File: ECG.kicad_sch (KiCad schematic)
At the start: 0 parts

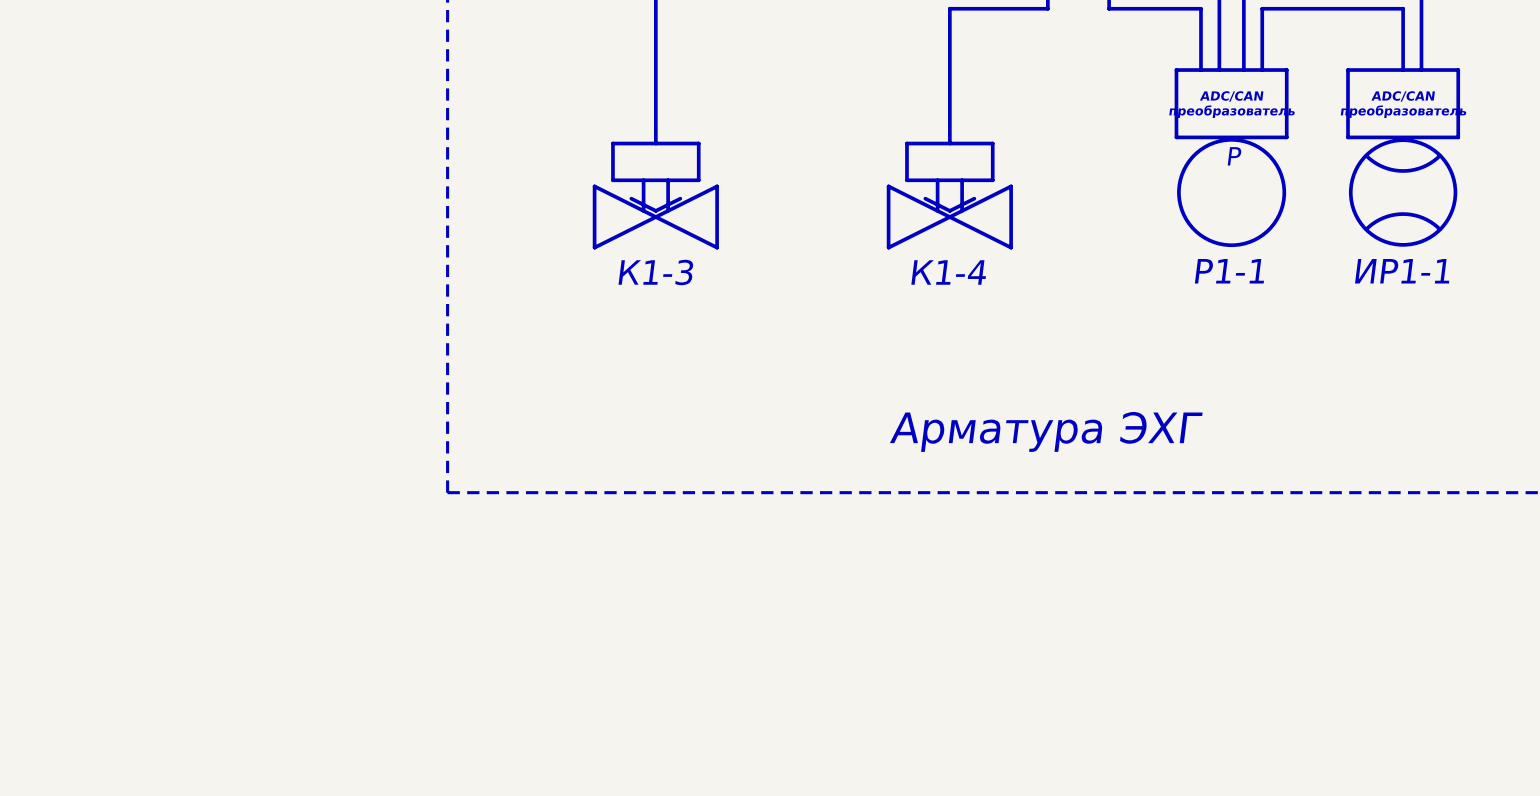
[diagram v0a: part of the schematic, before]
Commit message: VER1.0: добавил схему в пдф
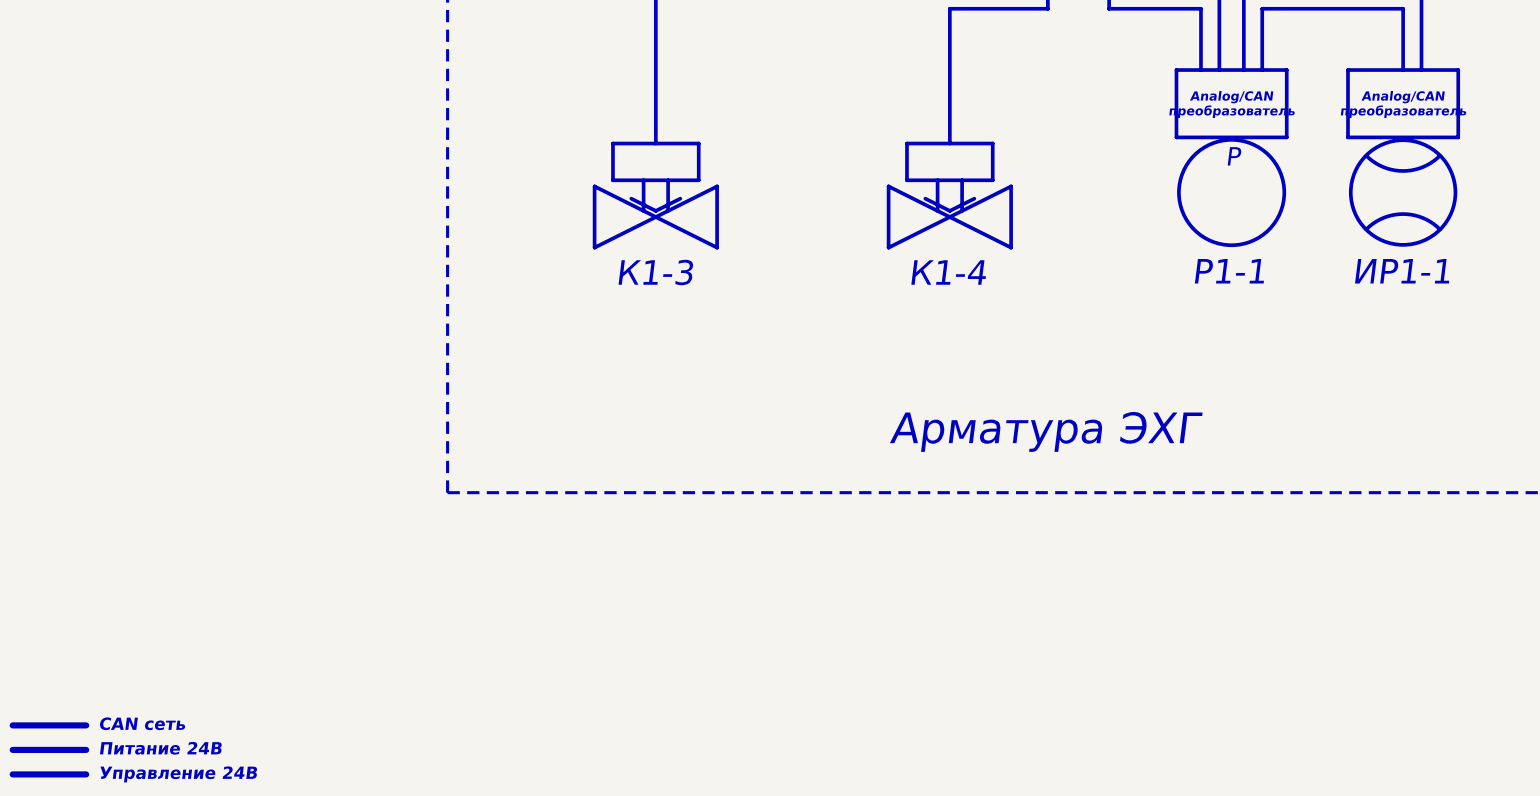
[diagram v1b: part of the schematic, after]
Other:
- note added: "Питание 24В"
- note added: "Управление 24В"
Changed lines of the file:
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@@
+		)
+	)
+	(text "Питание 24В"
+		(exclude_from_sim no)
+		(at 62.23 377.19 0)
+		(effects
+			(font
+				(face "Calibri")
+				(size 2.54 2.54)
+				(thickness 0.254)
+				(bold yes)
+				(italic yes)
+				(color 0 0 0 1)
+			)
+			(justify left)
 		)
 	)
@@
 		)
 	)
+	(text "Управление 24В"
+		(exclude_from_sim no)
+		(at 62.23 382.27 0)
+		(effects
+			(font
+				(face "Calibri")
+				(size 2.54 2.54)
+				(thickness 0.254)
+				(bold yes)
+				(italic yes)
+				(color 0 0 0 1)
+			)
+			(justify left)
+		)
+	)
+	(text "CAN сеть"
+		(exclude_from_sim no)
+		(at 62.23 372.11 0)
+		(effects
+			(font
+				(face "Calibri")
+				(size 2.54 2.54)
+				(thickness 0.254)
+				(bold yes)
+				(italic yes)
+				(color 0 0 0 1)
+			)
+			(justify left)
+		)
+	)
 	(text "ИР1-1"
 		(exclude_from_sim no)
@@
 		)
 	)
-	(text_box "ADC/CAN\nпреобразователь"
+	(text_box "Analog/CAN\nпреобразователь"
 		(exclude_from_sim no)
 		(at 321.31 236.22 0)
@@
 		)
 	)
-	(text_box "ADC/CAN\nпреобразователь"
+	(text_box "Analog/CAN\nпреобразователь"
 		(exclude_from_sim no)
 		(at 285.75 236.22 0)
@@
 	(polyline
 		(pts
+			(xy 44.45 382.27) (xy 59.69 382.27)
+		)
+		(stroke
+			(width 1.27)
+			(type solid)
+			(color 0 0 255 1)
+		)
+	)
+	(polyline
+		(pts
 			(xy 320.04 147.32) (xy 383.54 147.32)
 		)
@@
 	(polyline
 		(pts
+			(xy 44.45 372.11) (xy 59.69 372.11)
+		)
+		(stroke
+			(width 1.27)
+			(type solid)
+			(color 0 194 0 1)
+		)
+	)
+	(polyline
+		(pts
 			(xy 190.5 273.05) (xy 190.5 260.35)
 		)
@@
 		)
 	)
+	(polyline
+		(pts
+			(xy 44.45 377.19) (xy 59.69 377.19)
+		)
+		(stroke
+			(width 1.27)
+			(type solid)
+			(color 194 0 0 1)
+		)
+	)

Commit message: VER1.0: исправил часть замечаний по схеме
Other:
- note added: "220В"
- note added: "T"
- note added: "T2-1"
- note added: "Аналоговый сигнал"
- note added: "Напряжение переменное AC (сеть)"
- note added: "ЭН2-1"

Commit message: refactor for new ver
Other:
- note added: "Помещение 1"
- note added: "Помещение 2"
- note removed: "+24В"
- note removed: "Арматура ЭХГ"
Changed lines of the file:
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@@
+		)
+	)
+	(rectangle
+		(start 134.62 87.63)
+		(end 473.71 203.2)
+		(stroke
+			(width 0.635)
+			(type dash)
+			(color 0 0 0 1)
+		)
+		(fill
+			(type none)
 		)
 	)
@@
 		)
 	)
-	(text "+24В"
-		(exclude_from_sim no)
-		(at 350.52 160.528 0)
-		(effects
-			(font
-				(face "Calibri")
-				(size 3.81 3.81)
-				(italic yes)
-				(color 0 0 0 1)
-			)
-		)
-	)
 	(text "T2-1"
 		(exclude_from_sim no)
@@
 		)
 	)
+	(text "Помещение 1"
+		(exclude_from_sim no)
+		(at 435.864 100.33 0)
+		(effects
+			(font
+				(face "Calibri")
+				(size 6.35 6.35)
+				(italic yes)
+				(color 0 0 0 1)
+			)
+		)
+	)
 	(text "Напряжение переменное AC (сеть)"
 		(exclude_from_sim no)
@@
 		)
 	)
-	(text "CAN сеть"
-		(exclude_from_sim no)
-		(at 350.012 144.018 0)
-		(effects
-			(font
-				(face "Calibri")
-				(size 3.81 3.81)
-				(italic yes)
-				(color 0 0 0 1)
-			)
-		)
-	)
-	(text "Арматура ЭХГ"
-		(exclude_from_sim no)
-		(at 258.572 310.896 0)
+	(text "Помещение 2"
+		(exclude_from_sim no)
+		(at 440.436 316.23 0)
 		(effects
 			(font
@@
 	(text_box "Контроллер верхнего уровня (КВУ)"
 		(exclude_from_sim no)
-		(at 241.3 121.92 0)
+		(at 229.87 121.92 0)
 		(size 78.74 71.12)
 		(margins 0.9525 0.9525 0.9525 0.9525)
@@
 			(width 1.27)
 			(type solid)
-			(color 194 0 194 1)
+			(color 50 0 50 1)
 		)
 	)
@@
 	(polyline
 		(pts
-			(xy 320.04 163.83) (xy 383.54 163.83)
+			(xy 177.8 251.46) (xy 177.8 218.44)
+		)
+		(stroke
+			(width 0.762)
+			(type solid)
+		)
+	)
+	(polyline
+		(pts
+			(xy 44.45 382.27) (xy 59.69 382.27)
 		)
 		(stroke
 			(width 1.27)
 			(type solid)
-			(color 194 0 0 1)
-		)
-	)
-	(polyline
-		(pts
-			(xy 177.8 251.46) (xy 177.8 218.44)
-		)
-		(stroke
-			(width 0.762)
-			(type solid)
-		)
-	)
-	(polyline
-		(pts
-			(xy 44.45 382.27) (xy 59.69 382.27)
-		)
-		(stroke
-			(width 1.27)
-			(type solid)
 			(color 0 0 255 1)
 		)
 	)
-	(polyline
-		(pts
-			(xy 320.04 147.32) (xy 383.54 147.32)
-		)
-		(stroke
-			(width 1.27)
-			(type solid)
-			(color 0 194 0 1)
-		)
-	)

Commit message: version for piter
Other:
- note added: "Аналоговая цепь 2 х 1,5 кв.мм (например МКЭШ 1,5)"
- note added: "Питание 24В 2 x 1,5кв.мм (например, ПВС)"
- note added: "Управление 24В 2 х 1,5 кв.мм (например МКЭШ 1,5)"
- note removed: "Питание 24В"
- note removed: "Управление 24В"
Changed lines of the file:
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@@
 		)
 	)
-	(text "Питание 24В"
+	(text "Питание 24В 2 x 1,5кв.мм (например, ПВС)"
 		(exclude_from_sim no)
 		(at 62.23 377.19 0)
@@
 		)
 	)
+	(text "Помещение 2"
+		(exclude_from_sim no)
+		(at 435.864 100.33 0)
+		(effects
+			(font
+				(face "Calibri")
+				(size 6.35 6.35)
+				(italic yes)
+				(color 0 0 0 1)
+			)
+		)
+	)
+	(text "Напряжение переменное AC (сеть)"
+		(exclude_from_sim no)
+		(at 62.23 361.95 0)
+		(effects
+			(font
+				(face "Calibri")
+				(size 2.54 2.54)
+				(thickness 0.254)
+				(bold yes)
+				(italic yes)
+				(color 0 0 0 1)
+			)
+			(justify left)
+		)
+	)
+	(text "Р"
+		(exclude_from_sim no)
+		(at 297.434 254.508 0)
+		(effects
+			(font
+				(face "Calibri")
+				(size 3.81 3.81)
+				(italic yes)
+				(color 132 0 0 1)
+			)
+		)
+	)
+	(text "Аналоговый сигнал"
+		(exclude_from_sim no)
+		(at 62.23 367.03 0)
+		(effects
+			(font
+				(face "Calibri")
+				(size 2.54 2.54)
+				(thickness 0.254)
+				(bold yes)
+				(italic yes)
+				(color 0 0 0 1)
+			)
+			(justify left)
+		)
+	)
 	(text "Помещение 1"
 		(exclude_from_sim no)
-		(at 435.864 100.33 0)
+		(at 440.436 316.23 0)
 		(effects
 			(font
@@
 		)
 	)
-	(text "Напряжение переменное AC (сеть)"
-		(exclude_from_sim no)
-		(at 62.23 361.95 0)
-		(effects
-			(font
-				(face "Calibri")
-				(size 2.54 2.54)
-				(thickness 0.254)
-				(bold yes)
-				(italic yes)
-				(color 0 0 0 1)
-			)
-			(justify left)
-		)
-	)
-	(text "Р"
-		(exclude_from_sim no)
-		(at 297.434 254.508 0)
+	(text "К1-3"
+		(exclude_from_sim no)
+		(at 177.546 278.638 0)
+		(effects
+			(font
+				(face "Calibri")
+				(size 5.08 5.08)
+				(italic yes)
+				(color 132 0 0 1)
+			)
+		)
+	)
+	(text "К1-4"
+		(exclude_from_sim no)
+		(at 238.252 278.638 0)
+		(effects
+			(font
+				(face "Calibri")
+				(size 5.08 5.08)
+				(italic yes)
+				(color 132 0 0 1)
+			)
+		)
+	)
+	(text "220В"
+		(exclude_from_sim no)
+		(at 486.156 238.506 0)
 		(effects
 			(font
@@
 				(size 3.81 3.81)
 				(italic yes)
-				(color 132 0 0 1)
-			)
-		)
-	)
-	(text "Аналоговый сигнал"
-		(exclude_from_sim no)
-		(at 62.23 367.03 0)
-		(effects
-			(font
-				(face "Calibri")
-				(size 2.54 2.54)
-				(thickness 0.254)
-				(bold yes)
-				(italic yes)
-				(color 0 0 0 1)
-			)
-			(justify left)
-		)
-	)
-	(text "Помещение 2"
-		(exclude_from_sim no)
-		(at 440.436 316.23 0)
-		(effects
-			(font
-				(face "Calibri")
-				(size 6.35 6.35)
-				(italic yes)
-				(color 0 0 0 1)
-			)
-		)
-	)
-	(text "К1-3"
-		(exclude_from_sim no)
-		(at 177.546 278.638 0)
-		(effects
-			(font
-				(face "Calibri")
-				(size 5.08 5.08)
-				(italic yes)
-				(color 132 0 0 1)
-			)
-		)
-	)
-	(text "К1-4"
-		(exclude_from_sim no)
-		(at 238.252 278.638 0)
-		(effects
-			(font
-				(face "Calibri")
-				(size 5.08 5.08)
-				(italic yes)
-				(color 132 0 0 1)
-			)
-		)
-	)
-	(text "220В"
-		(exclude_from_sim no)
-		(at 486.156 238.506 0)
+				(color 0 0 0 1)
+			)
+		)
+	)
+	(text "T"
+		(exclude_from_sim no)
+		(at 372.11 255.27 0)
 		(effects
 			(font
@@
 				(size 3.81 3.81)
 				(italic yes)
-				(color 0 0 0 1)
-			)
-		)
-	)
-	(text "T"
-		(exclude_from_sim no)
-		(at 372.11 255.27 0)
-		(effects
-			(font
-				(face "Calibri")
-				(size 3.81 3.81)
-				(italic yes)
-				(color 132 0 0 1)
-			)
-		)
-	)
-	(text "Управление 24В"
+				(color 132 0 0 1)
+			)
+		)
+	)
+	(text "Управление 24В 2 х 1,5 кв.мм (например МКЭШ 1,5)"
 		(exclude_from_sim no)
 		(at 62.23 382.27 0)
@@
 				(color 132 0 0 1)
 			)
+		)
+	)
+	(text "Аналоговая цепь 2 х 1,5 кв.мм (например МКЭШ 1,5)"
+		(exclude_from_sim no)
+		(at 61.976 388.112 0)
+		(effects
+			(font
+				(face "Calibri")
+				(size 2.54 2.54)
+				(thickness 0.254)
+				(bold yes)
+				(italic yes)
+				(color 0 0 0 1)
+			)
+			(justify left)
 		)
 	)
@@
 		)
 	)
+	(polyline
+		(pts
+			(xy 44.45 387.35) (xy 59.69 387.35)
+		)
+		(stroke
+			(width 1.27)
+			(type solid)
+			(color 72 72 72 1)
+		)
+	)

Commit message: VER1.0: добавил датчик электропроводности
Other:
- note added: "QA"
- note added: "QA1-1"
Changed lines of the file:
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@@
 	(generator_version "10.0")
 	(paper "A2")
+	(circle
+		(center 270.256 261.112)
+		(radius 10.925)
+		(stroke
+			(width 0.762)
+			(type solid)
+			(color 132 0 0 1)
+		)
+		(fill
+			(type none)
+		)
+	)
 	(rectangle
 		(start 168.91 251.46)
@@
 	(rectangle
 		(start 134.62 208.28)
-		(end 473.71 323.85)
+		(end 496.57 323.85)
 		(stroke
 			(width 0.635)
@@
 	(rectangle
 		(start 134.62 87.63)
-		(end 473.71 203.2)
+		(end 496.57 203.2)
 		(stroke
 			(width 0.635)
@@
 		)
 	)
+	(text "QA1-1"
+		(exclude_from_sim no)
+		(at 269.748 277.876 0)
+		(effects
+			(font
+				(face "Calibri")
+				(size 5.08 5.08)
+				(italic yes)
+				(color 132 0 0 1)
+			)
+		)
+	)
 	(text "T2-1"
 		(exclude_from_sim no)
@@
 		)
 	)
+	(text "QA"
+		(exclude_from_sim no)
+		(at 270.51 254 0)
+		(effects
+			(font
+				(face "Calibri")
+				(size 3.81 3.81)
+				(italic yes)
+				(color 132 0 0 1)
+			)
+		)
+	)
 	(text_box "Контроллер верхнего уровня (КВУ)"
 		(exclude_from_sim no)
@@
 	(polyline
 		(pts
+			(xy 270.51 193.04) (xy 270.51 222.25)
+		)
+		(stroke
+			(width 0.762)
+			(type solid)
+			(color 72 72 72 1)
+		)
+	)
+	(polyline
+		(pts
 			(xy 416.56 265.43) (xy 422.91 259.08)
 		)
@@
 		(pts
 			(xy 276.86 193.04) (xy 276.86 222.25)
+		)
+		(stroke
+			(width 0.762)
+			(type solid)
+			(color 72 72 72 1)
+		)
+	)
+	(polyline
+		(pts
+			(xy 270.51 222.25) (xy 270.51 250.19)
 		)
 		(stroke
@@
 	)
 	(group ""
+		(members "275ecefa-ee0c-4be6-99d9-43ee472bc265" "fb40584c-c175-4a28-85a1-fee45963e35b")
+	)
+	(group ""
